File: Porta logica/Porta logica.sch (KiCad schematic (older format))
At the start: 56 parts, among them P1 Input, P2 Batteria, P3 Out, SW1 SW_PUSH, SW2 SW_PUSH, U1 74HC595, U2 7805, U3 74HC595, U4 74HC00, U5 74HC595

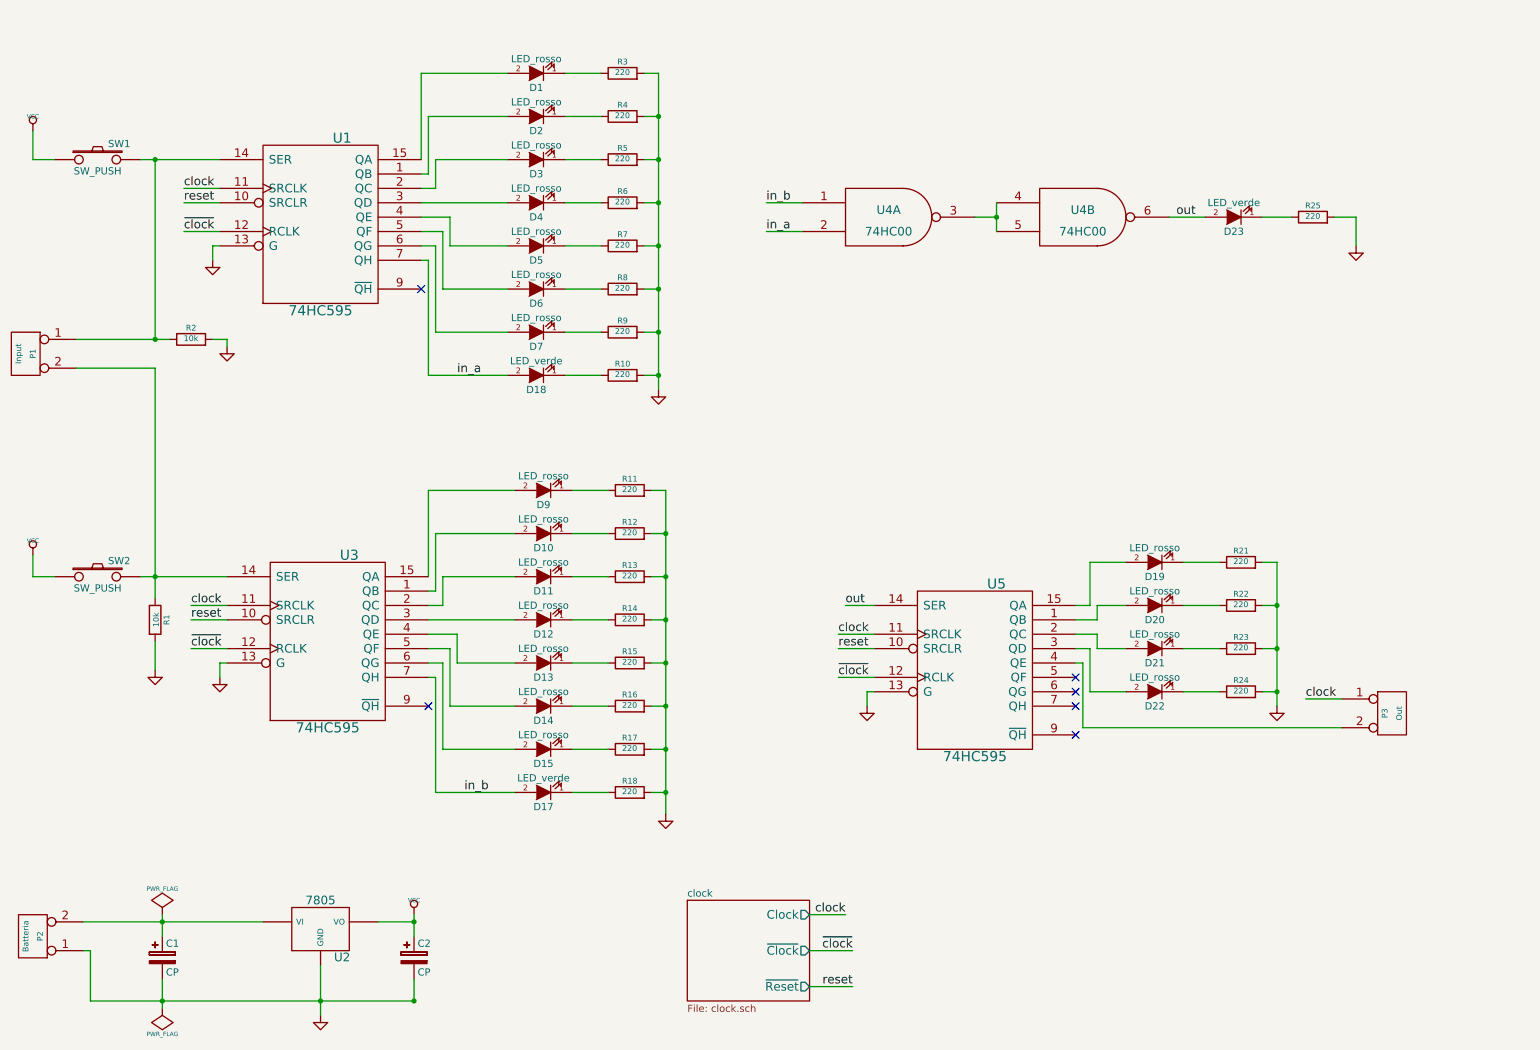
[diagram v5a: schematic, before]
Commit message: Ripulito schematico, migliorato associazioni
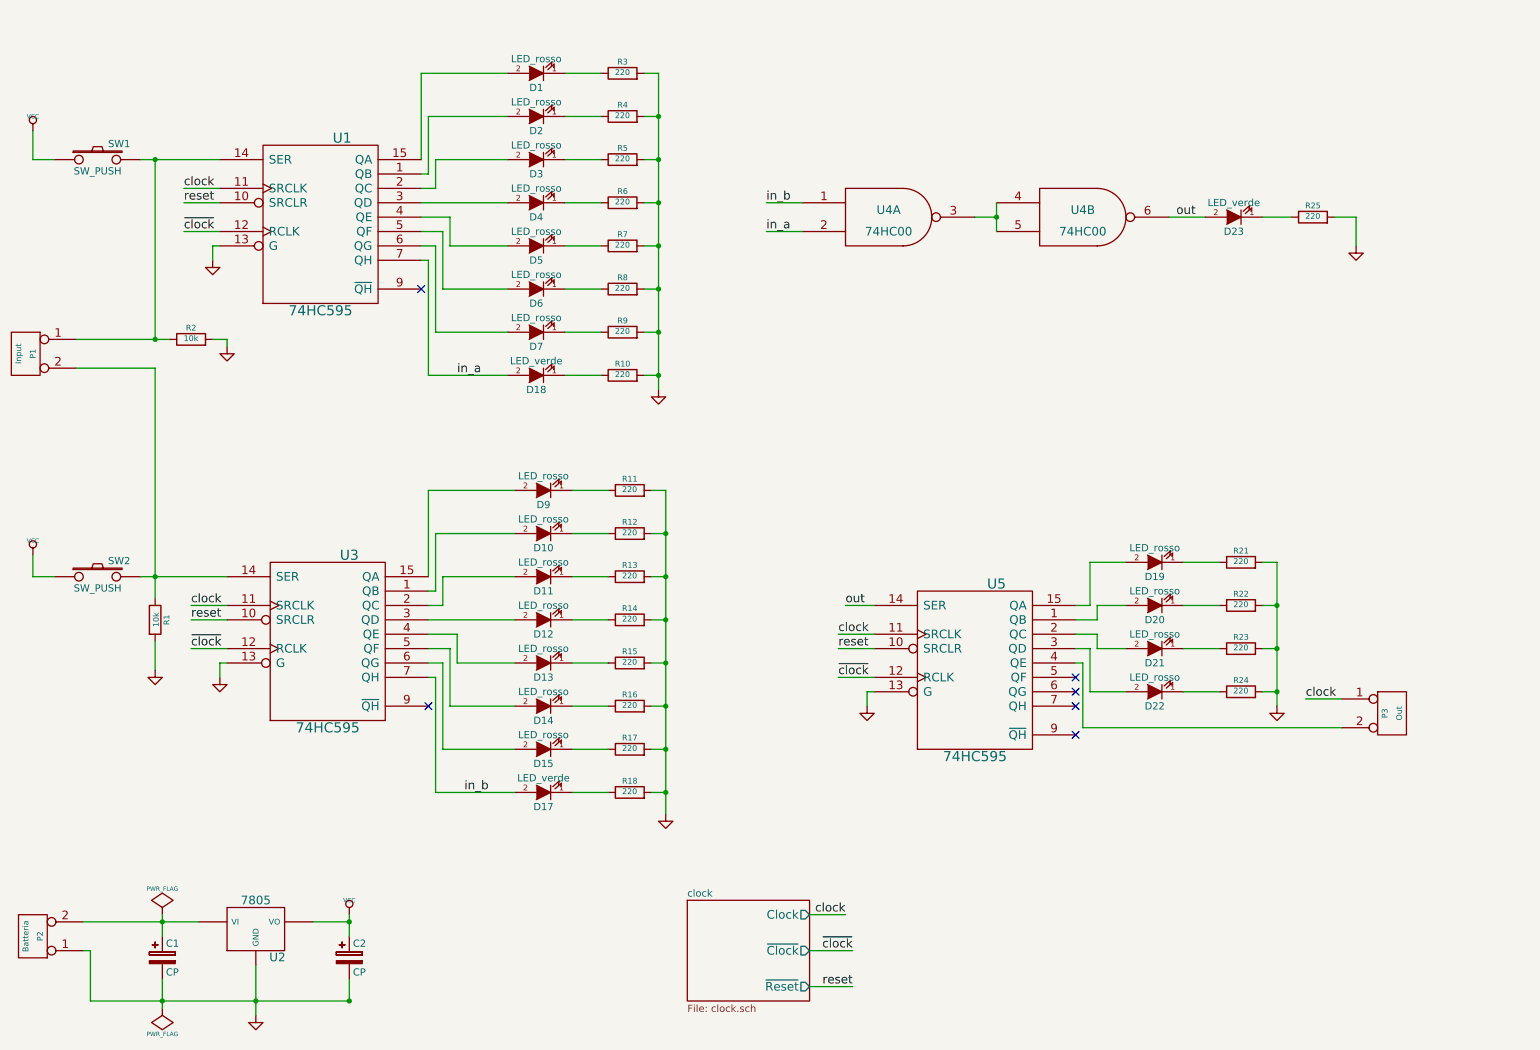
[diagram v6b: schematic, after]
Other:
- moved on the sheet: C2, U2
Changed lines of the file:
@@
 $EndComp
 $Comp
-L GND #PWR9
+L GND #PWR01
 U 1 1 555B2D83
 P 5100 3200
-F 0 "#PWR9" H 5100 3200 30  0001 C CNN
+F 0 "#PWR01" H 5100 3200 30  0001 C CNN
 F 1 "GND" H 5100 3130 30  0001 C CNN
 F 2 "" H 5100 3200 60  0000 C CNN
@@
 $EndComp
 $Comp
-L GND #PWR10
+L GND #PWR02
 U 1 1 555B2EBC
 P 5150 6150
-F 0 "#PWR10" H 5150 6150 30  0001 C CNN
+F 0 "#PWR02" H 5150 6150 30  0001 C CNN
 F 1 "GND" H 5150 6080 30  0001 C CNN
 F 2 "" H 5150 6150 60  0000 C CNN
@@
 $EndComp
 $Comp
-L GND #PWR4
+L GND #PWR03
 U 1 1 555B387E
 P 2000 2300
-F 0 "#PWR4" H 2000 2300 30  0001 C CNN
+F 0 "#PWR03" H 2000 2300 30  0001 C CNN
 F 1 "GND" H 2000 2230 30  0001 C CNN
 F 2 "" H 2000 2300 60  0000 C CNN
@@
 $EndComp
 $Comp
-L GND #PWR5
+L GND #PWR04
 U 1 1 555B3C44
 P 2050 5200
-F 0 "#PWR5" H 2050 5200 30  0001 C CNN
+F 0 "#PWR04" H 2050 5200 30  0001 C CNN
 F 1 "GND" H 2050 5130 30  0001 C CNN
 F 2 "" H 2050 5200 60  0000 C CNN
@@
 $EndComp
 $Comp
-L VCC #PWR2
+L VCC #PWR05
 U 1 1 555B3F08
 P 750 4350
-F 0 "#PWR2" H 750 4450 30  0001 C CNN
+F 0 "#PWR05" H 750 4450 30  0001 C CNN
 F 1 "VCC" H 750 4450 30  0000 C CNN
 F 2 "" H 750 4350 60  0000 C CNN
@@
 $EndComp
 $Comp
-L GND #PWR3
+L GND #PWR06
 U 1 1 555B3F85
 P 1600 5150
-F 0 "#PWR3" H 1600 5150 30  0001 C CNN
+F 0 "#PWR06" H 1600 5150 30  0001 C CNN
 F 1 "GND" H 1600 5080 30  0001 C CNN
 F 2 "" H 1600 5150 60  0000 C CNN
@@
 $EndComp
 $Comp
-L VCC #PWR1
+L VCC #PWR07
 U 1 1 555B4214
 P 750 1400
-F 0 "#PWR1" H 750 1500 30  0001 C CNN
+F 0 "#PWR07" H 750 1500 30  0001 C CNN
 F 1 "VCC" H 750 1500 30  0000 C CNN
 F 2 "" H 750 1400 60  0000 C CNN
@@
 $EndComp
 $Comp
-L GND #PWR15
+L GND #PWR08
 U 1 1 555B4D13
 P 9950 2200
-F 0 "#PWR15" H 9950 2200 30  0001 C CNN
+F 0 "#PWR08" H 9950 2200 30  0001 C CNN
 F 1 "GND" H 9950 2130 30  0001 C CNN
 F 2 "" H 9950 2200 60  0000 C CNN
@@
 $EndComp
 $Comp
-L GND #PWR11
+L GND #PWR09
 U 1 1 555B7A84
 P 6550 5400
-F 0 "#PWR11" H 6550 5400 30  0001 C CNN
+F 0 "#PWR09" H 6550 5400 30  0001 C CNN
 F 1 "GND" H 6550 5330 30  0001 C CNN
 F 2 "" H 6550 5400 60  0000 C CNN
@@
 NoConn ~ 8000 5200
 $Comp
-L GND #PWR14
+L GND #PWR010
 U 1 1 555B7DFC
 P 9400 5400
-F 0 "#PWR14" H 9400 5400 30  0001 C CNN
+F 0 "#PWR010" H 9400 5400 30  0001 C CNN
 F 1 "GND" H 9400 5330 30  0001 C CNN
 F 2 "" H 9400 5400 60  0000 C CNN
@@
 	6150 7350 6450 7350
 Wire Wire Line
-	1500 1600 2050 1600
+	1500 1600 1600 1600
+Wire Wire Line
+	1600 1600 2050 1600
 Connection ~ 9400 5300
 Connection ~ 9400 5000
@@
 Connection ~ 5100 1300
 Wire Wire Line
-	9400 4400 9400 5400
+	9400 4400 9400 4700
+Wire Wire Line
+	9400 4700 9400 5000
+Wire Wire Line
+	9400 5000 9400 5300
+Wire Wire Line
+	9400 5300 9400 5400
 Wire Wire Line
 	8100 5300 8350 5300
@@
 Connection ~ 7450 2000
 Wire Wire Line
-	7450 1900 7450 2100
+	7450 1900 7450 2000
+Wire Wire Line
+	7450 2000 7450 2100
 Wire Wire Line
 	7300 2000 7450 2000
@@
 Connection ~ 1600 4500
 Wire Wire Line
-	1500 4500 2100 4500
+	1500 4500 1600 4500
+Wire Wire Line
+	1600 4500 2100 4500
 Connection ~ 1600 1600
 Wire Wire Line
 	1600 4950 1600 5150
 Wire Wire Line
-	1600 3050 1600 4650
+	1600 3050 1600 4500
+Wire Wire Line
+	1600 4500 1600 4650
 Wire Wire Line
 	750  4500 900  4500
@@
 	3500 4500 3500 3900
 Wire Wire Line
-	5150 3900 5150 6150
+	5150 3900 5150 4200
+Wire Wire Line
+	5150 4200 5150 4500
+Wire Wire Line
+	5150 4500 5150 4800
+Wire Wire Line
+	5150 4800 5150 5100
+Wire Wire Line
+	5150 5100 5150 5400
+Wire Wire Line
+	5150 5400 5150 5700
+Wire Wire Line
+	5150 5700 5150 6000
+Wire Wire Line
+	5150 6000 5150 6150
 Wire Wire Line
 	4500 3900 4750 3900
@@
 	3450 1600 3450 1000
 Wire Wire Line
-	5100 1000 5100 3200
+	5100 1000 5100 1300
+Wire Wire Line
+	5100 1300 5100 1600
+Wire Wire Line
+	5100 1600 5100 1900
+Wire Wire Line
+	5100 1900 5100 2200
+Wire Wire Line
+	5100 2200 5100 2500
+Wire Wire Line
+	5100 2500 5100 2800
+Wire Wire Line
+	5100 2800 5100 3100
+Wire Wire Line
+	5100 3100 5100 3200
 Wire Wire Line
 	4450 1000 4700 1000
@@
 	1600 1600 1600 2850
 Wire Wire Line
-	1050 2850 1700 2850
+	1050 2850 1600 2850
+Wire Wire Line
+	1600 2850 1700 2850
 Wire Wire Line
 	6400 4700 6600 4700
@@
 $EndComp
 Wire Wire Line
-	2750 7200 2750 7550
-Connection ~ 2750 7450
-Wire Wire Line
-	3400 7450 3400 7300
-Connection ~ 3400 7450
-Wire Wire Line
-	1650 6850 1650 7000
+	2300 7200 2300 7450
+Wire Wire Line
+	2300 7450 2300 7550
+Connection ~ 2300 7450
+Wire Wire Line
+	2950 7450 2950 7300
+Connection ~ 2950 7450
+Wire Wire Line
+	1650 6850 1650 6900
+Wire Wire Line
+	1650 6900 1650 7000
 Connection ~ 1650 6900
 Wire Wire Line
-	1650 7300 1650 7500
+	1650 7300 1650 7450
+Wire Wire Line
+	1650 7450 1650 7500
 Connection ~ 1650 7450
 $Comp
-L GND #PWR7
+L GND #PWR011
 U 1 1 555F4257
-P 2750 7550
-F 0 "#PWR7" H 2750 7550 30  0001 C CNN
-F 1 "GND" H 2750 7480 30  0001 C CNN
-F 2 "" H 2750 7550 60  0000 C CNN
-F 3 "" H 2750 7550 60  0000 C CNN
-	1    2750 7550
-	1    0    0    -1
-$EndComp
-Wire Wire Line
-	1100 6900 2350 6900
+P 2300 7550
+F 0 "#PWR011" H 2300 7550 30  0001 C CNN
+F 1 "GND" H 2300 7480 30  0001 C CNN
+F 2 "" H 2300 7550 60  0000 C CNN
+F 3 "" H 2300 7550 60  0000 C CNN
+	1    2300 7550
+	1    0    0    -1
+$EndComp
+Wire Wire Line
+	1100 6900 1650 6900
+Wire Wire Line
+	1650 6900 1900 6900
 Wire Wire Line
 	1100 7100 1150 7100
@@
 	1150 7100 1150 7450
 Wire Wire Line
-	3400 6850 3400 7000
-Connection ~ 3400 6900
-$Comp
-L PWR_FLAG #FLG1
+	2950 6850 2950 6900
+Wire Wire Line
+	2950 6900 2950 7000
+Connection ~ 2950 6900
+$Comp
+L PWR_FLAG #FLG012
 U 1 1 555F4263
 P 1650 6850
-F 0 "#FLG1" H 1650 6945 30  0001 C CNN
+F 0 "#FLG012" H 1650 6945 30  0001 C CNN
 F 1 "PWR_FLAG" H 1650 7030 30  0000 C CNN
 F 2 "" H 1650 6850 60  0000 C CNN
@@
 $EndComp
 $Comp
-L PWR_FLAG #FLG2
+L PWR_FLAG #FLG013
 U 1 1 555F4269
 P 1650 7500
-F 0 "#FLG2" H 1650 7595 30  0001 C CNN
+F 0 "#FLG013" H 1650 7595 30  0001 C CNN
 F 1 "PWR_FLAG" H 1650 7680 30  0000 C CNN
 F 2 "" H 1650 7500 60  0000 C CNN
@@
 L CP C2
 U 1 1 555F47B5
-P 3400 7150
-F 0 "C2" H 3425 7250 50  0000 L CNN
-F 1 "CP" H 3425 7050 50  0000 L CNN
-F 2 "Capacitors_Elko_ThroughHole:Elko_vert_11.2x6.3mm_RM2.5" H 3438 7000 30  0001 C CNN
-F 3 "" H 3400 7150 60  0000 C CNN
-	1    3400 7150
-	1    0    0    -1
-$EndComp
-Wire Wire Line
-	1150 7450 3400 7450
-$Comp
-L VCC #PWR8
+P 2950 7150
+F 0 "C2" H 2975 7250 50  0000 L CNN
+F 1 "CP" H 2975 7050 50  0000 L CNN
+F 2 "Capacitors_Elko_ThroughHole:Elko_vert_11.2x6.3mm_RM2.5" H 2988 7000 30  0001 C CNN
+F 3 "" H 2950 7150 60  0000 C CNN
+	1    2950 7150
+	1    0    0    -1
+$EndComp
+Wire Wire Line
+	1150 7450 1650 7450
+Wire Wire Line
+	1650 7450 2300 7450
+Wire Wire Line
+	2300 7450 2950 7450
+$Comp
+L VCC #PWR014
 U 1 1 555F5AA1
-P 3400 6850
-F 0 "#PWR8" H 3400 6950 30  0001 C CNN
-F 1 "VCC" H 3400 6950 30  0000 C CNN
-F 2 "" H 3400 6850 60  0000 C CNN
-F 3 "" H 3400 6850 60  0000 C CNN
-	1    3400 6850
-	1    0    0    -1
-$EndComp
-Wire Wire Line
-	3150 6900 3400 6900
+P 2950 6850
+F 0 "#PWR014" H 2950 6950 30  0001 C CNN
+F 1 "VCC" H 2950 6950 30  0000 C CNN
+F 2 "" H 2950 6850 60  0000 C CNN
+F 3 "" H 2950 6850 60  0000 C CNN
+	1    2950 6850
+	1    0    0    -1
+$EndComp
+Wire Wire Line
+	2700 6900 2950 6900
 $Comp
 L 7805 U2
 U 1 1 555F1A27
-P 2750 6950
-F 0 "U2" H 2900 6754 60  0000 C CNN
-F 1 "7805" H 2750 7150 60  0000 C CNN
-F 2 "Housings_SOIC:SOIC-16_7.5x10.3mm_Pitch1.27mm" H 2750 6950 60  0001 C CNN
-F 3 "" H 2750 6950 60  0000 C CNN
-	1    2750 6950
+P 2300 6950
+F 0 "U2" H 2450 6754 60  0000 C CNN
+F 1 "7805" H 2300 7150 60  0000 C CNN
+F 2 "Housings_SOIC:SOIC-16_7.5x10.3mm_Pitch1.27mm" H 2300 6950 60  0001 C CNN
+F 3 "" H 2300 6950 60  0000 C CNN
+	1    2300 6950
 	1    0    0    -1
 $EndComp
@@
 	5850 1900 6100 1900
 $Comp
-L GND #PWR?
+L GND #PWR015
 U 1 1 555FB14F
 P 2100 2900
-F 0 "#PWR?" H 2100 2900 30  0001 C CNN
+F 0 "#PWR015" H 2100 2900 30  0001 C CNN
 F 1 "GND" H 2100 2830 30  0001 C CNN
 F 2 "" H 2100 2900 60  0000 C CNN
